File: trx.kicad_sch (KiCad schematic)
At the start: 34 parts, among them IC31 BK4802P, J31 NM, J51 Conn_Coaxial, X31 Crystal

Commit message: Add files via upload
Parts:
- C31, C36, C38: value 1u -> 0.1u
- C35: value 27p -> 22p
- C39: value 27p -> 33p
- C45: value NM -> 0.1u
- C52, C54: value 4p -> 22p
- C53: value 22p -> 18p
- L51, L52: value 50n -> 20n
- R34: value 10k -> NM
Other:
- note added: "5mm 1.5T"
- note added: "R32 Yaesu 4.7k Standard 22k ICOM 22k KENWOOD open"
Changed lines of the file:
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@@
     (stroke (width 0) (type default))
   )
+  (text "R32\nYaesu      4.7k\nStandard   22k\nICOM       22k\nKENWOOD  open"
+    (at 91.44 166.37 0)
+    (effects (font (size 1.27 1.27)) (justify left bottom))
+  )
+  (text "5mm 1.5T" (at 215.9 31.75 0)
+    (effects (font (size 1.27 1.27)) (justify left bottom))
+  )
   (text "Ver2022.2 Jumper\nC14 - R13(+3.3V)" (at 34.29 68.58 0)
+    (effects (font (size 1.27 1.27)) (justify left bottom))
+  )
+  (text "5mm 1.5T" (at 160.02 31.75 0)
     (effects (font (size 1.27 1.27)) (justify left bottom))
   )
@@
       (effects (font (size 1.27 1.27)))
     )
-    (property "Value" "1u" (at 105.41 69.5706 90)
+    (property "Value" "0.1u" (at 105.41 69.5706 90)
       (effects (font (size 1.27 1.27)))
     )
@@
       (effects (font (size 1.27 1.27)) (justify left))
     )
-    (property "Value" "1u" (at 62.611 68.453 0)
+    (property "Value" "0.1u" (at 62.611 68.453 0)
       (effects (font (size 1.27 1.27)) (justify left))
     )
@@
       (effects (font (size 1.27 1.27)))
     )
-    (property "Value" "10k" (at 160.02 68.1736 90)
+    (property "Value" "NM" (at 160.02 68.1736 90)
       (effects (font (size 1.27 1.27)))
     )
@@
       (effects (font (size 1.27 1.27)) (justify left))
     )
-    (property "Value" "27p" (at 104.521 100.203 0)
+    (property "Value" "22p" (at 104.521 100.203 0)
       (effects (font (size 1.27 1.27)) (justify left))
     )
@@
       (effects (font (size 1.27 1.27)) (justify left))
     )
-    (property "Value" "27p" (at 124.841 100.203 0)
+    (property "Value" "33p" (at 124.841 100.203 0)
       (effects (font (size 1.27 1.27)) (justify left))
     )
@@
       (effects (font (size 1.27 1.27)))
     )
-    (property "Value" "1u" (at 116.84 67.0306 90)
+    (property "Value" "0.1u" (at 116.84 67.0306 90)
       (effects (font (size 1.27 1.27)))
     )
@@
       (effects (font (size 1.27 1.27)) (justify left))
     )
-    (property "Value" "4p" (at 208.153 36.449 0)
+    (property "Value" "22p" (at 208.153 36.449 0)
       (effects (font (size 1.27 1.27)) (justify left))
     )
@@
       (effects (font (size 1.27 1.27)) (justify left))
     )
-    (property "Value" "50n" (at 220.853 38.0238 0)
+    (property "Value" "20n" (at 220.853 38.0238 0)
       (effects (font (size 1.27 1.27)) (justify left))
     )
@@
       (effects (font (size 1.27 1.27)) (justify left))
     )
-    (property "Value" "NM" (at 159.131 134.493 0)
+    (property "Value" "0.1u" (at 159.131 134.493 0)
       (effects (font (size 1.27 1.27)) (justify left))
     )
@@
       (effects (font (size 1.27 1.27)))
     )
-    (property "Value" "22p" (at 187.6806 45.72 90)
+    (property "Value" "18p" (at 187.6806 45.72 90)
       (effects (font (size 1.27 1.27)))
     )
@@
       (effects (font (size 1.27 1.27)) (justify left))
     )
-    (property "Value" "4p" (at 178.943 36.449 0)
+    (property "Value" "22p" (at 178.943 36.449 0)
       (effects (font (size 1.27 1.27)) (justify left))
     )
@@
       (effects (font (size 1.27 1.27)) (justify left))
     )
-    (property "Value" "50n" (at 164.973 38.0238 0)
-      (effects (font (size 1.27 1.27)) (justify left))
-    )
+    (property "Value" "20n" (at 164.973 38.0238 0)
+      (effects (font (size 1.27 1.27)) (justify left))
+    )

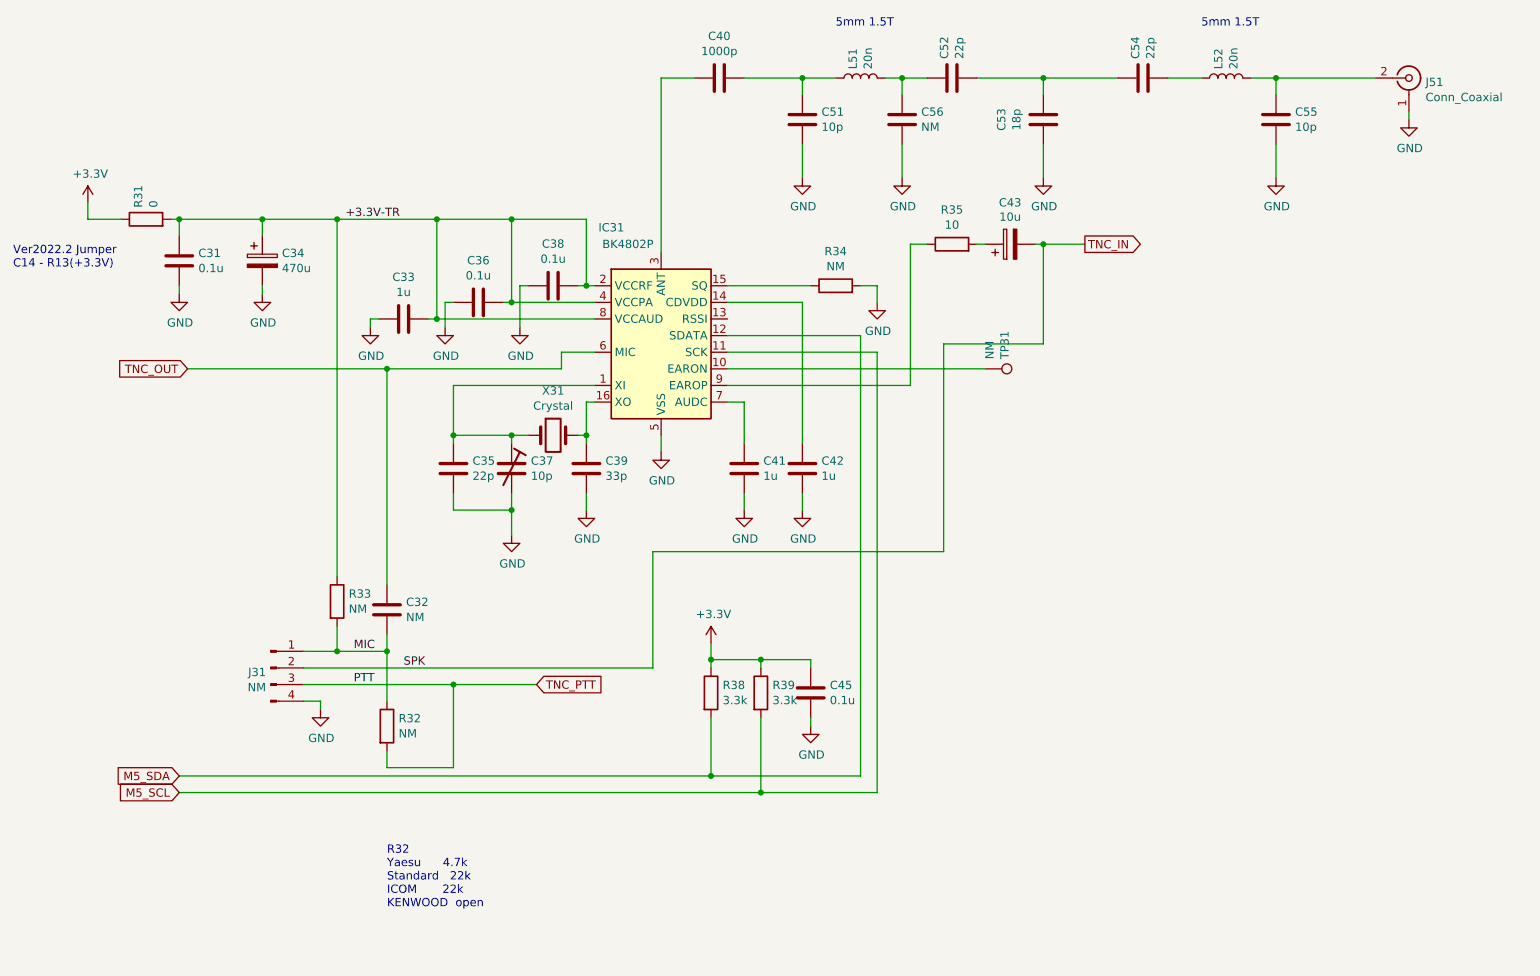
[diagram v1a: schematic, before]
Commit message: CAD data update
CADデータを更新
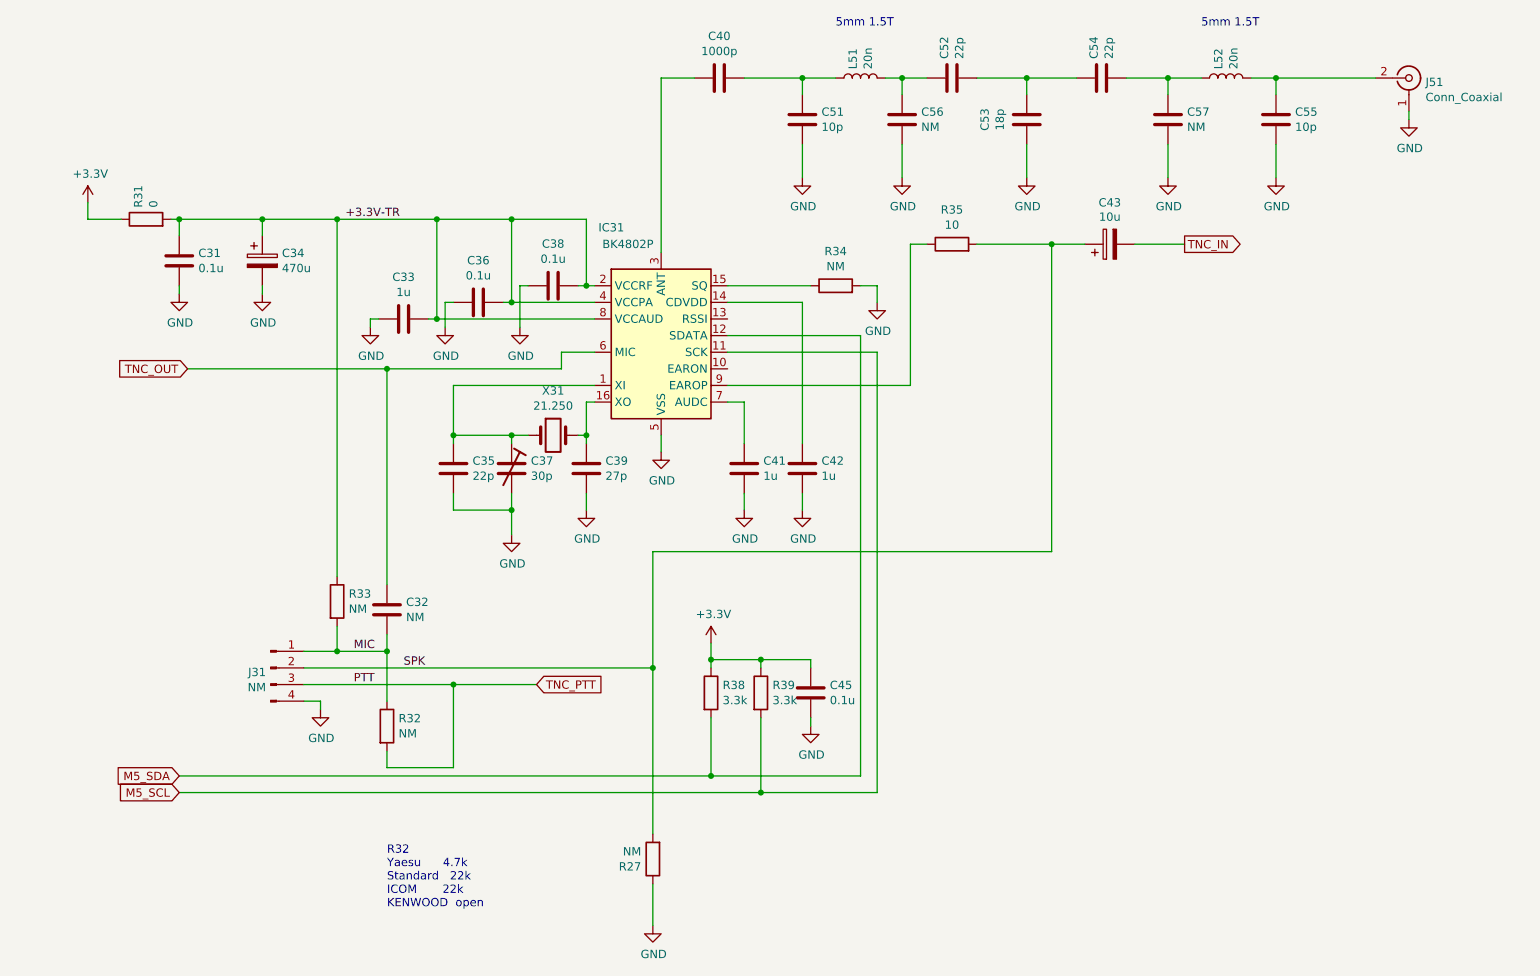
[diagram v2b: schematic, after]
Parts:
- removed TP31: NM, usr-Library:PinHeader_1x01, symbol Connector:TestPoint
- added C57: NM, Capacitor_THT:C_Disc_D3.4mm_W2.1mm_P2.50mm, symbol Device:C
- added R27: NM, Resistor_THT:R_Axial_DIN0207_L6.3mm_D2.5mm_P2.54mm_Vertical, symbol Device:R
- C37: value 10p -> 30p
- C39: value 33p -> 27p
- X31: value Crystal -> 21.250
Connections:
- net GND: now also C57.2, R27.1
- net TNC_IN: no longer J31.2 (Pin_2)
- net SPK: now reaches C43.1, R35.2
- net SPK: now also J31.2 (Pin_2), R27.2
- net at C54.2, L52.1: now also C57.1
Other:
- note removed: "Ver2022.2 Jumper C14 - R13(+3.3V)"
- moved on the sheet: C43, C53, C54

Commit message: Add files via upload
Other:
- note added: "R32 Yaesu 2.2k Standard 22k ICOM 22k KENWOOD open"
- note removed: "R32 Yaesu 4.7k Standard 22k ICOM 22k KENWOOD open"
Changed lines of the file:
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@@
   (title_block
     (title "QRP-TNC")
-    (date "2022-05-03")
+    (date "2023-08-13")
     (company "PRUG / JK1MLY")
   )
@@
     (stroke (width 0) (type default))
   )
-  (text "R32\nYaesu      4.7k\nStandard   22k\nICOM       22k\nKENWOOD  open"
+  (text "R32\nYaesu      2.2k\nStandard   22k\nICOM       22k\nKENWOOD  open"
     (at 91.44 166.37 0)
     (effects (font (size 1.27 1.27)) (justify left bottom))
@@
       (effects (font (size 1.27 1.27)) hide)
     )
-    (property "Datasheet" "digikey 0805CS-3N3EJTS" (at 219.71 39.37 0)
+    (property "Datasheet" "1.5T" (at 219.71 39.37 0)
       (effects (font (size 1.27 1.27)) hide)
     )
@@
       (effects (font (size 1.27 1.27)) hide)
     )
-    (property "Datasheet" "digikey 0805CS-3N3EJTS" (at 163.83 39.37 0)
-      (effects (font (size 1.27 1.27)) hide)
-    )
+    (property "Datasheet" "1.5T" (at 163.83 39.37 0)
+      (effects (font (size 1.27 1.27)) hide)
+    )
